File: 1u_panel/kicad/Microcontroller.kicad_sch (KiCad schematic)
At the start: 43 parts, among them J2 ORESAT-DEBUG-CONNECTOR-ALL, U1 TCAN330, U11 TMP101NA/3KSLOTTED, U2 TMP101NA/3KSLOTTED, U7 STM32F091C, X1 CRYSTAL-WITH-GND

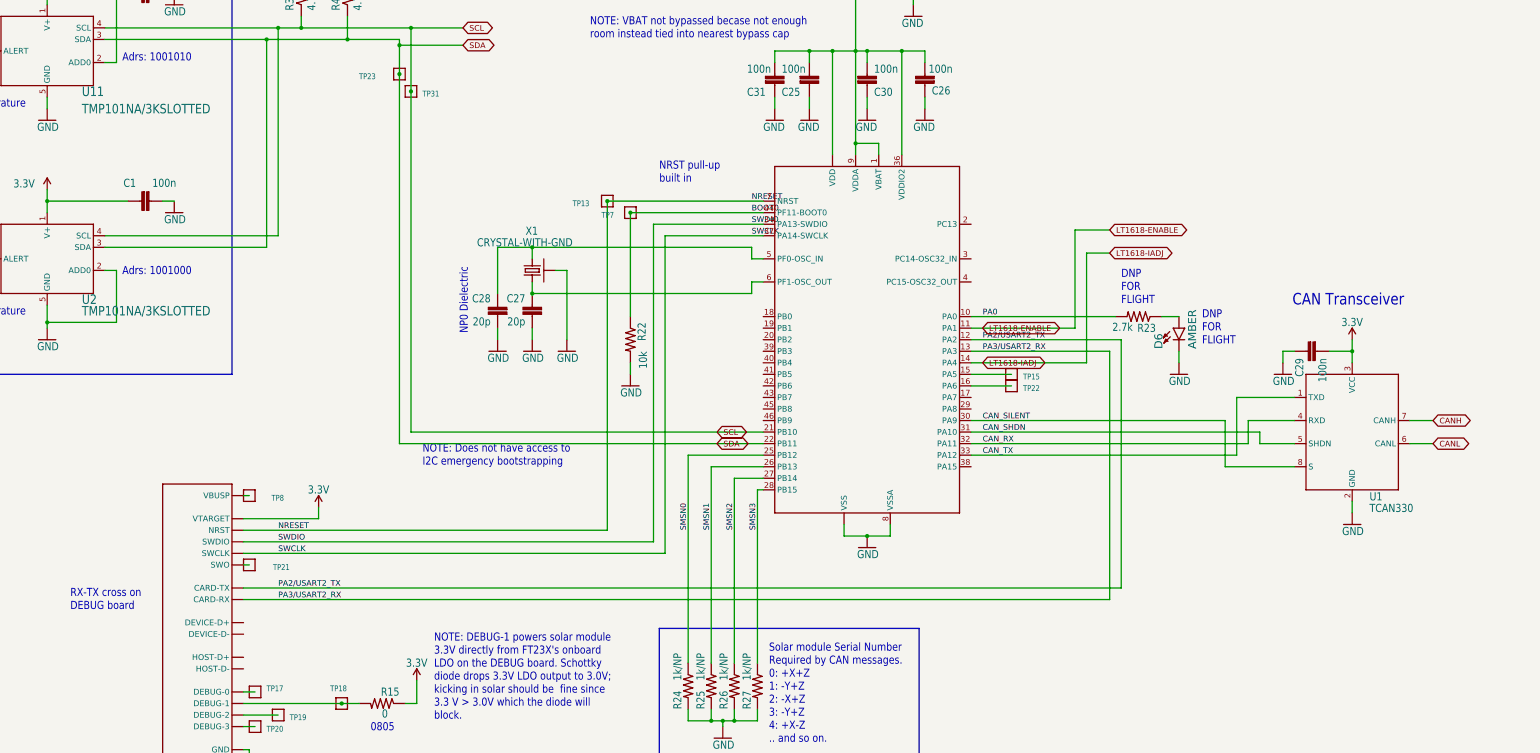
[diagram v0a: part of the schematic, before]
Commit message: Cleaned up schematic; added correct values and part numbers, added datasheet links to important components, imported sch to brd, LOTS of errors to clean up there but it's at synced now.
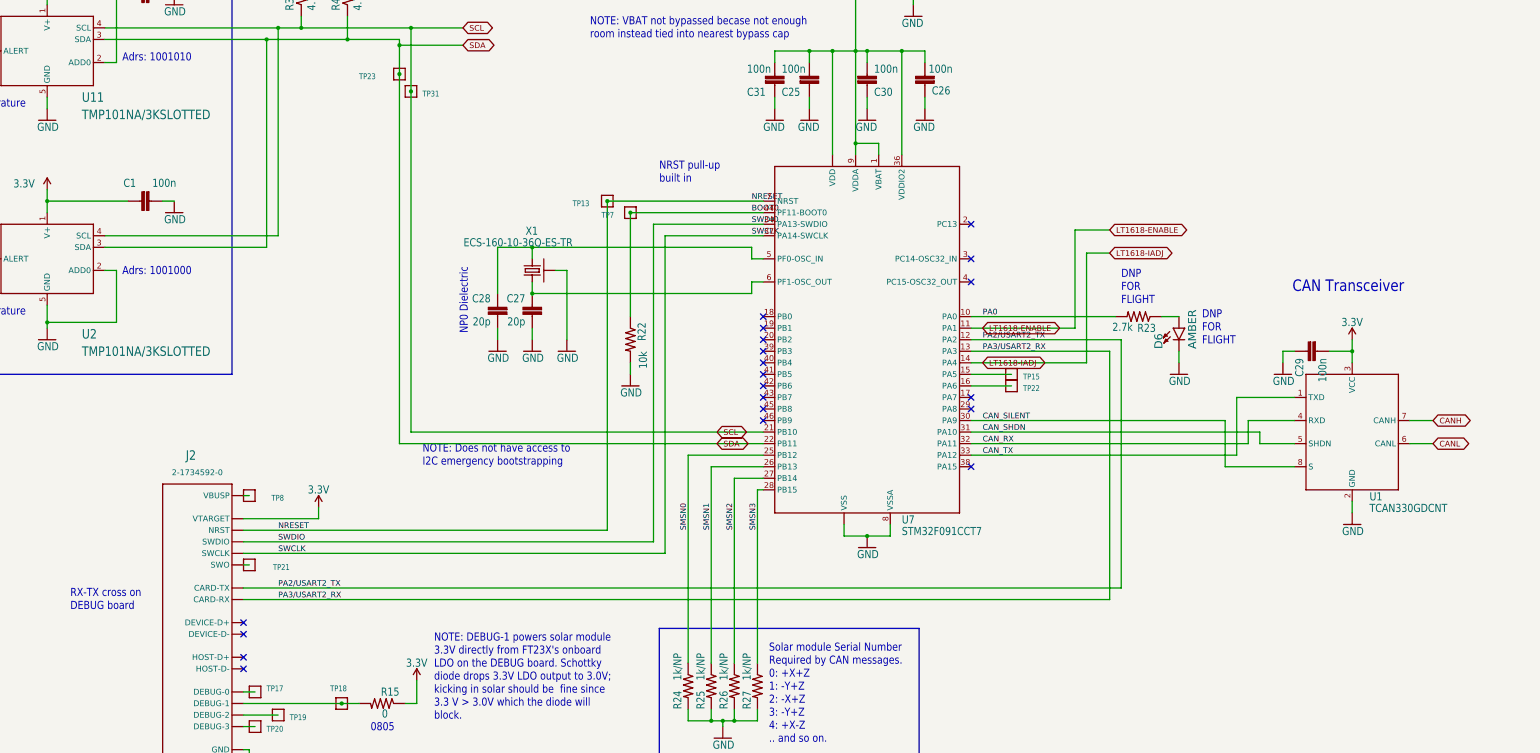
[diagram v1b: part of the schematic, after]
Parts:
- J2: value ORESAT-DEBUG-CONNECTOR-ALL -> 2-1734592-0
- U1: value TCAN330 -> TCAN330GDCNT
- U7: value STM32F091C -> STM32F091CCT7
- X1: value CRYSTAL-WITH-GND -> ECS-160-10-36Q-ES-TR
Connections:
- no-connect marks 0 -> 20
